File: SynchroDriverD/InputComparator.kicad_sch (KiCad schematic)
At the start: 12 parts, among them U2 LM324, U4 74LV14

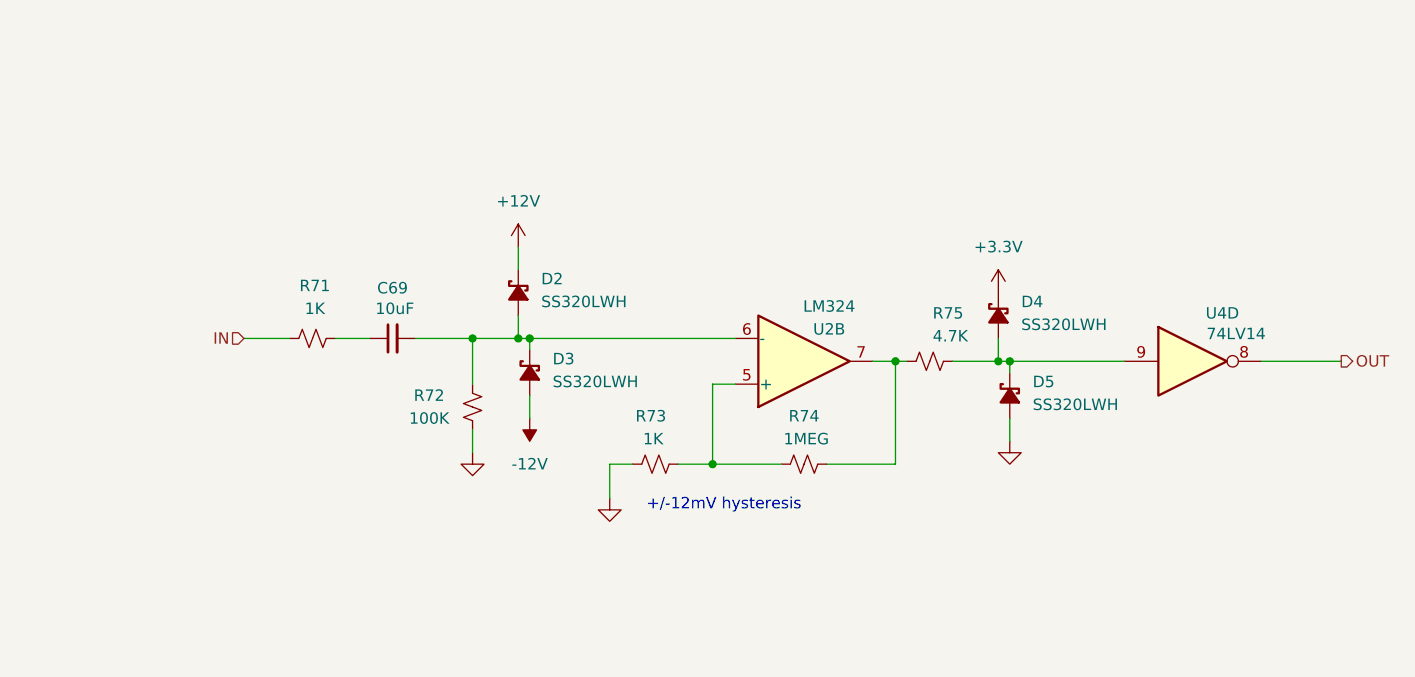
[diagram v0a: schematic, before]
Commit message: Swap DRV8300 for DRV8300DI, change ref in
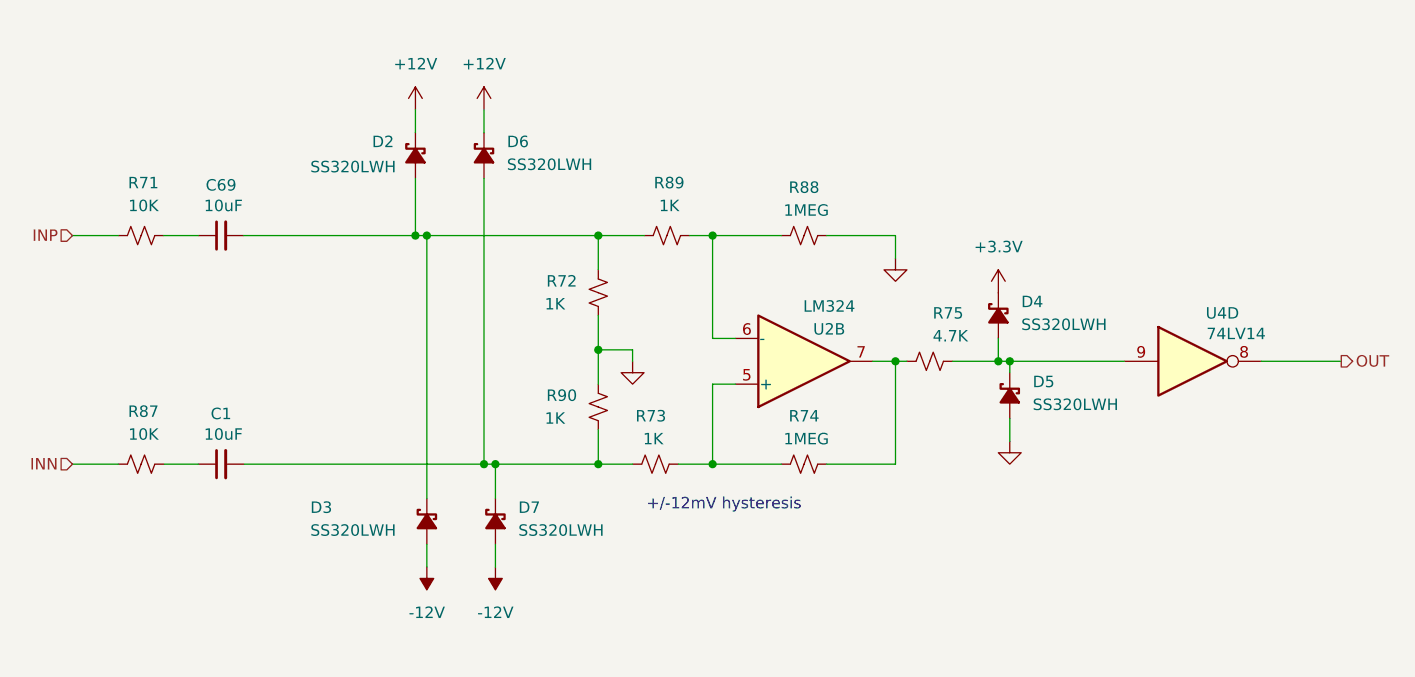
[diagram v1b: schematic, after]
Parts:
- added C1: 10uF, Capacitor_SMD:C_1206_3216Metric, symbol Device:C_Small
- added D6, D7: SS320LWH, Active:SOD3716X117, symbol Device:D_Schottky_Small_Filled
- added R87: 10K, Passive:RESC3216X70, symbol Device:R_Small_US
- added R88: 1MEG, Passive:RESC1608X55, symbol Device:R_Small_US
- added R89: 1K, Passive:RESC3216X70, symbol Device:R_Small_US
- added R90: 1K, Passive:RESC1608X55, symbol Device:R_Small_US
- R71: value 1K -> 10K
- R72: value 100K -> 1K
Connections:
- net +12V: now also D6.1 (K)
- net -12V: now also D7.2 (A)
- net GND: now also R88.1, R90.1; no longer R73.2
- net at C69.2, D2.2 (A), D3.1 (K)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: now also R89.1; no longer U2.6 (-)
- net IN renamed INP
- new net: R88.2, R89.2, U2.6 (-)
- new net: C1.2, D6.2 (A), D7.1 (K), R73.2, R90.2
- new net: C1.1, R87.2
- new net INN: R87.1
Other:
- moved on the sheet: C69, D2, D3, R71, R72

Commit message: Improve ref in, clearance for 115V
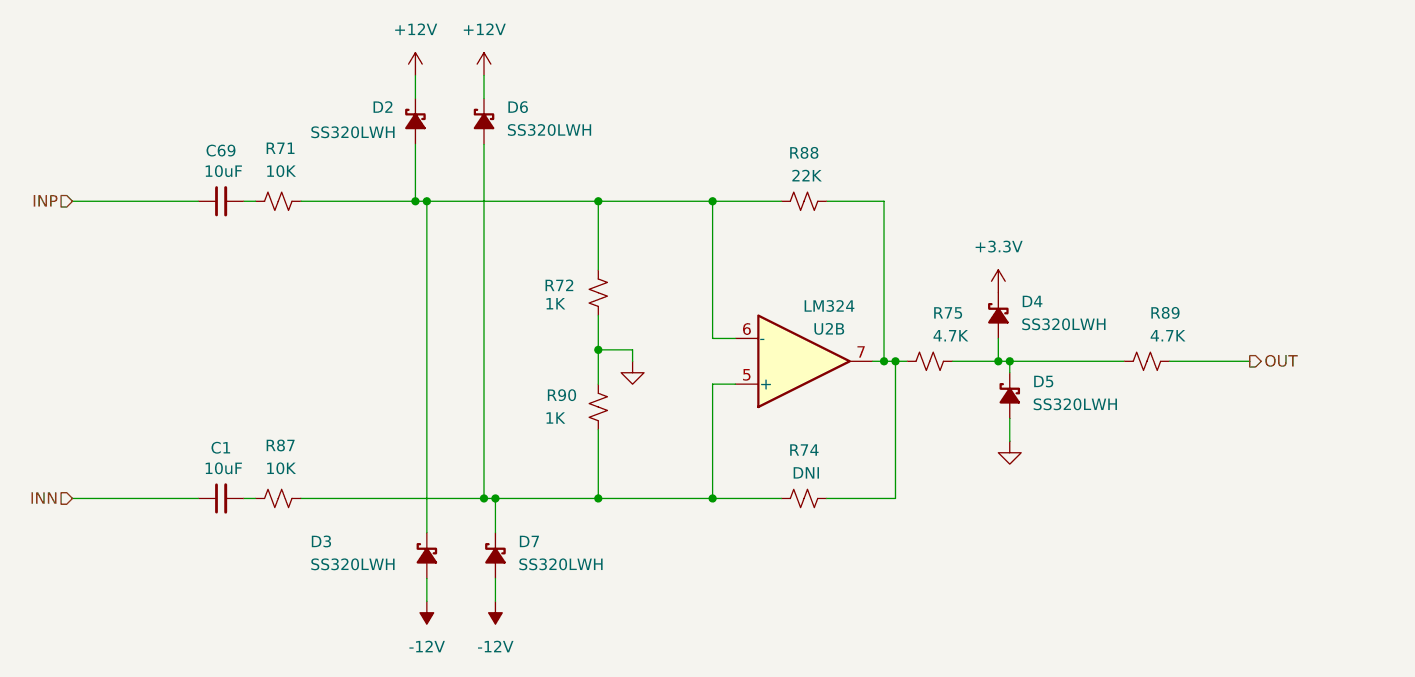
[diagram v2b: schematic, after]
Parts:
- removed R73: 1K, Passive:RESC1608X55, symbol Device:R_Small_US
- removed U4: 74LV14, Active:SOP127P620X175-14, symbol 74xx:74LV14
- R74: value 1MEG -> DNI
- R88: value 1MEG -> 22K
- R89: value 1K -> 4.7K; footprint Passive:RESC3216X70 -> Passive:RESC1608X55
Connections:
- net GND: no longer R88.1
- net INN: now also C1.1; no longer R87.1
- net INP: now also C69.1; no longer R71.1
- net OUT: now also R89.1
- net at D4.2 (A), D5.1 (K), R75.1: now also R89.2
- net at D2.2 (A), D3.1 (K), R72.1: now also R71.2, R88.2, U2.6 (-); no longer C69.2, R89.1
- net at R74.1, R75.2, U2.7: now also R88.1
- net at R74.2, U2.5 (+): now also D6.2 (A), D7.1 (K), R87.2, R90.2
- new net: C1.2, R87.1
- new net: C69.2, R71.1
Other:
- note removed: "+/-12mV hysteresis"
- moved on the sheet: C1, C69, D2, D3, D6, D7, R71, R74, R87, R88

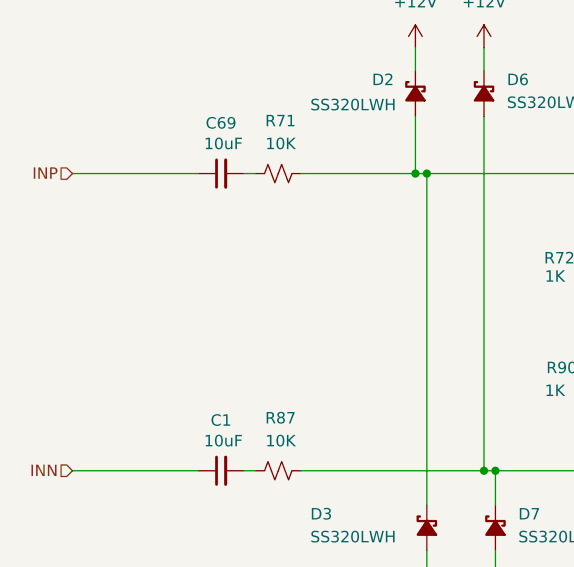
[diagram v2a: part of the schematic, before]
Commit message: Tweaks after first build
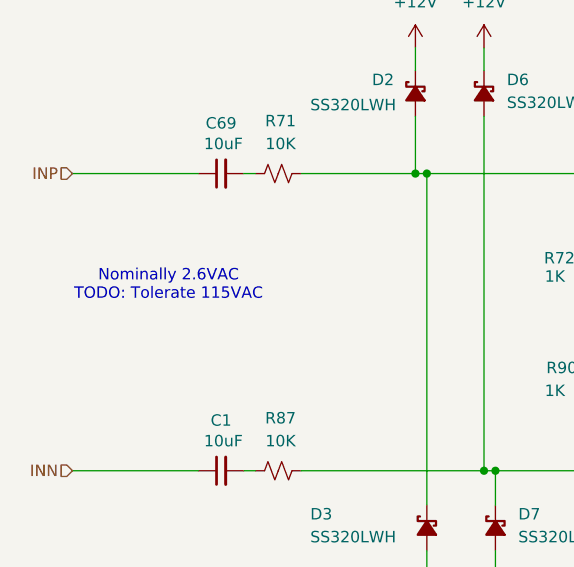
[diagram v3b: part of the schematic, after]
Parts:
- C1, C69: Mouser (none) -> 187-CL31A106KBHNNNE
- U2: Mouser (none) -> 863-LM324DR2G
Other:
- note added: "Nominally 2.6VAC TODO: Tolerate 115VAC"
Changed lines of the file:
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@@
 	(generator_version "9.0")
 	(paper "A4")
+	(text "Nominally 2.6VAC\nTODO: Tolerate 115VAC"
+		(exclude_from_sim no)
+		(at 43.688 77.216 0)
+		(effects
+			(font
+				(size 1.27 1.27)
+			)
+		)
+	)
 	(junction
 		(at 78.74 97.79)
@@
 			)
 		)
+		(property "Mouser" "863-LM324DR2G"
+			(at 114.3 82.55 0)
+			(effects
+				(font
+					(size 1.27 1.27)
+				)
+				(hide yes)
+			)
+		)
 		(pin "1"
 		)
@@
 			)
 		)
+		(property "Mouser" "187-CL31A106KBHNNNE"
+			(at 49.53 97.79 0)
+			(effects
+				(font
+					(size 1.27 1.27)
+				)
+				(hide yes)
+			)
+		)
 		(pin "2"
 		)
@@
 			(at 49.53 64.77 0)
 			(effects
+				(font
+					(size 1.27 1.27)
+				)
+				(hide yes)
+			)
+		)
+		(property "Mouser" "187-CL31A106KBHNNNE"
+			(at 49.53 64.77 0)
+			(effects

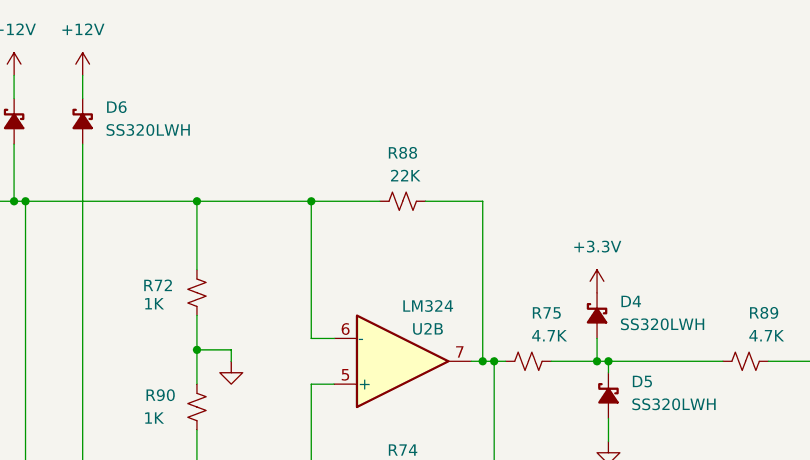
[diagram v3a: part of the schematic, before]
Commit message: Meter driver vref fix. Sync in gain fix.
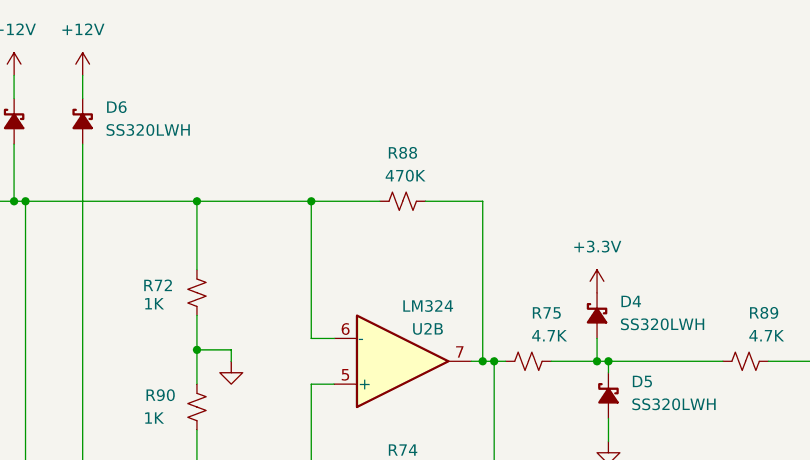
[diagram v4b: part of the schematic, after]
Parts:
- R88: value 22K -> 470K
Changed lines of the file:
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@@
 			)
 		)
-		(property "Value" "22K"
+		(property "Value" "470K"
 			(at 114.554 61.976 90)
 			(effects
